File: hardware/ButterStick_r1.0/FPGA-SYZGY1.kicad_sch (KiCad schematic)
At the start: 4 parts, among them U4 ECP5UM5G_85_CABGA381

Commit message: hw.r1d0: Update BOM fieids in schematic.
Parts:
- C158, C28: Mfg Samsung Electro-Mechanics -> Yageo; PN CL05B103KP5NNNC -> CC0402KRX5R6BB104; SN-DK 1276-1002-1-ND -> (none); Tol (none) -> 10V / X5R
- C27: Mfg Samsung Electro-Mechanics -> Yageo; PN CL05B104KP5NNNC -> CC0402KRX5R5BB474; SN-DK 1276-1002-1-ND -> (none)
- U4: Mfg (none) -> Lattice Semiconductor Corporation; PN (none) -> LFE5UM5G-85F-8BG381C; manf# ECP5UM5G_85 -> (none)
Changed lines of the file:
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@@
 (kicad_sch (version 20200618) (host eeschema "5.99.0-unknown-73168a9~101~ubuntu18.04.1")
-  (page 10 18)
+  (page 1 18)
   (paper "A4")
   (title_block
@@
       (effects (font (size 1.27 1.27)) hide)
     )
-    (property "SN-DK" "1276-1002-1-ND" (id 4) (at 16.51 246.38 0)
-      (effects (font (size 1.27 1.27)) hide)
-    )
-    (property "PN" "CL05B104KP5NNNC" (id 5) (at 16.51 246.38 0)
-      (effects (font (size 1.27 1.27)) hide)
-    )
-    (property "Mfg" "Samsung Electro-Mechanics" (id 6) (at 19.05 245.11 0)
+    (property "SN-DK" "" (id 4) (at 16.51 246.38 0)
+      (effects (font (size 1.27 1.27)) hide)
+    )
+    (property "PN" "CC0402KRX5R5BB474" (id 5) (at 16.51 246.38 0)
+      (effects (font (size 1.27 1.27)) hide)
+    )
+    (property "Mfg" "Yageo" (id 6) (at 19.05 245.11 0)
       (effects (font (size 1.27 1.27)) hide)
     )
@@
       (effects (font (size 1.27 1.27)) hide)
     )
-    (property "SN-DK" "1276-1002-1-ND" (id 4) (at 26.67 246.38 0)
-      (effects (font (size 1.27 1.27)) hide)
-    )
-    (property "PN" "CL05B103KP5NNNC" (id 5) (at 26.67 246.38 0)
-      (effects (font (size 1.27 1.27)) hide)
-    )
-    (property "Mfg" "Samsung Electro-Mechanics" (id 6) (at 19.05 245.11 0)
+    (property "SN-DK" "" (id 4) (at 26.67 246.38 0)
+      (effects (font (size 1.27 1.27)) hide)
+    )
+    (property "PN" "CC0402KRX5R6BB104" (id 5) (at 26.67 246.38 0)
+      (effects (font (size 1.27 1.27)) hide)
+    )
+    (property "Mfg" "Yageo" (id 6) (at 19.05 245.11 0)
+      (effects (font (size 1.27 1.27)) hide)
+    )
+    (property "Tol" "10V / X5R" (id 4) (at 176.53 69.85 0)
       (effects (font (size 1.27 1.27)) hide)
     )
@@
       (effects (font (size 1.27 1.27)) hide)
     )
-    (property "SN-DK" "1276-1002-1-ND" (id 4) (at 36.83 246.38 0)
-      (effects (font (size 1.27 1.27)) hide)
-    )
-    (property "PN" "CL05B103KP5NNNC" (id 5) (at 36.83 246.38 0)
-      (effects (font (size 1.27 1.27)) hide)
-    )
-    (property "Mfg" "Samsung Electro-Mechanics" (id 6) (at 29.21 245.11 0)
+    (property "SN-DK" "" (id 4) (at 36.83 246.38 0)
+      (effects (font (size 1.27 1.27)) hide)
+    )
+    (property "PN" "CC0402KRX5R6BB104" (id 5) (at 36.83 246.38 0)
+      (effects (font (size 1.27 1.27)) hide)
+    )
+    (property "Mfg" "Yageo" (id 6) (at 29.21 245.11 0)
+      (effects (font (size 1.27 1.27)) hide)
+    )
+    (property "Tol" "10V / X5R" (id 4) (at 186.69 69.85 0)
       (effects (font (size 1.27 1.27)) hide)
     )
@@
       (effects (font (size 1.524 1.524)) (justify right) hide)
     )
-    (property "manf#" "ECP5UM5G_85" (id 4) (at 123.19 72.39 0)
+    (property "manf#" "" (id 4) (at 123.19 72.39 0)
       (effects (font (size 1.524 1.524)) (justify right) hide)
     )
-  )
+    (property "Mfg" "Lattice Semiconductor Corporation" (id 4) (at 119.38 71.12 0)
+      (effects (font (size 1.27 1.27)) hide)
+    )
+    (property "PN" "LFE5UM5G-85F-8BG381C" (id 5) (at 119.38 71.12 0)
+      (effects (font (size 1.27 1.27)) hide)
+    )
+  )

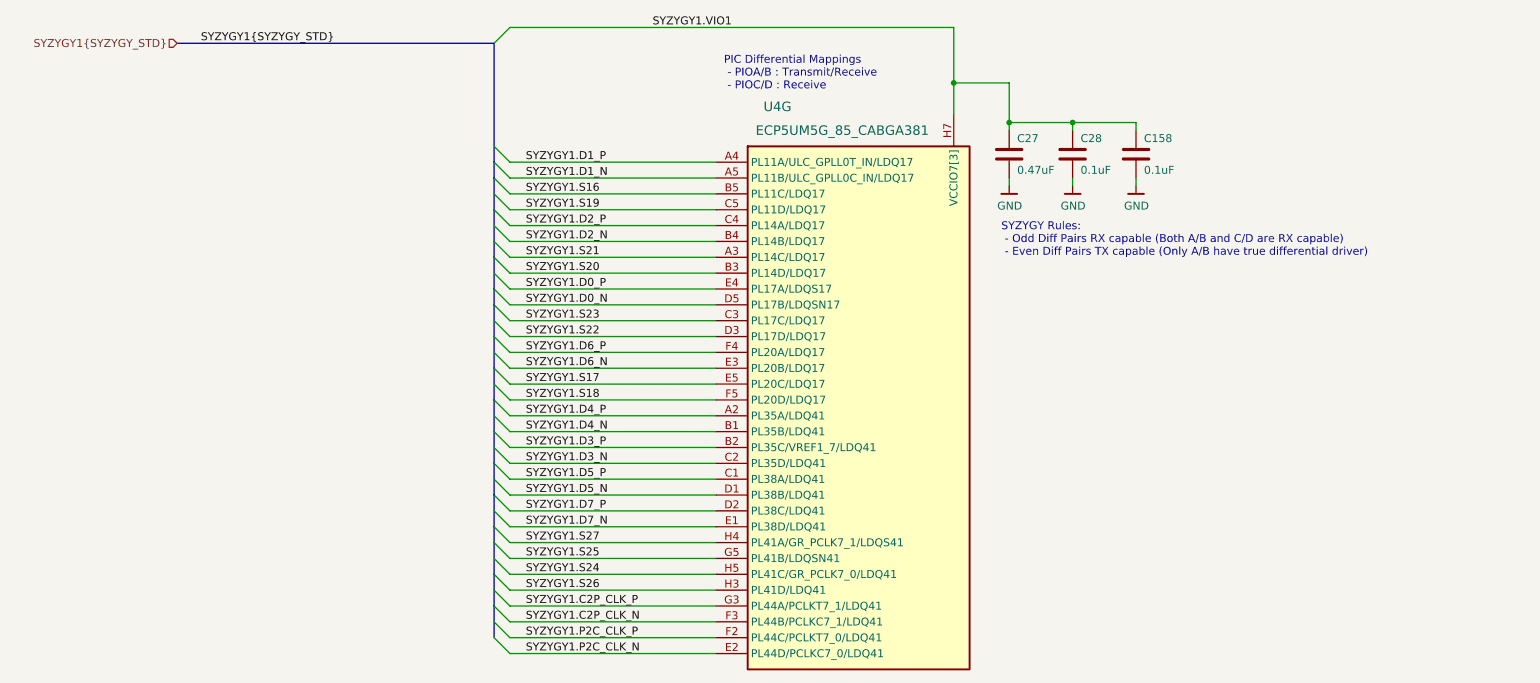
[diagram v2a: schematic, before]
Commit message: hw.r1d0: Fix RGMII straps
This commit correctly sets the stop resistos on the RGMII lines to 1K5
instead of DNP.
Also regenerate and add a schematic in PDF format.

Fixes #6
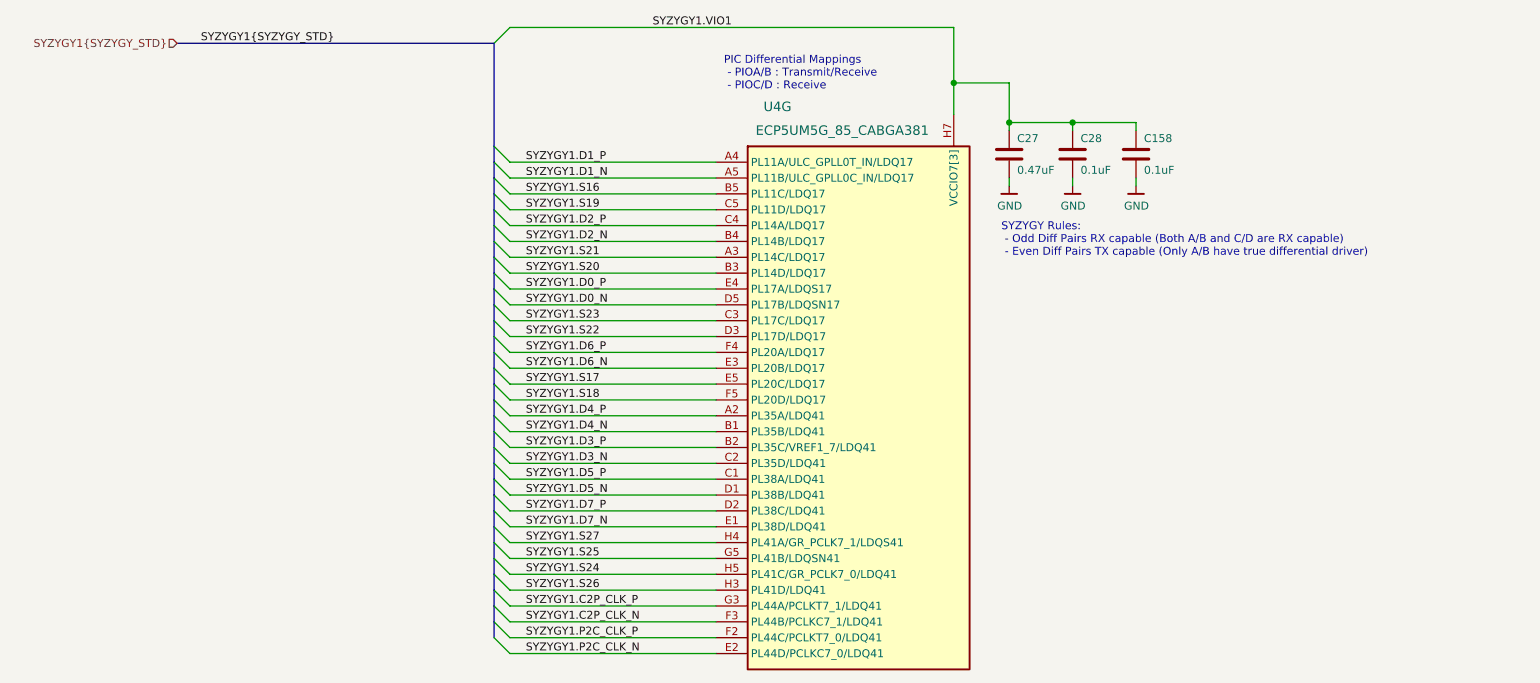
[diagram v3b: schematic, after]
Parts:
- U4: PN LFE5UM5G-85F-8BG381C -> LFE5UM5G-85F-8BG381I
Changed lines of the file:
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@@
-(kicad_sch (version 20200618) (host eeschema "5.99.0-unknown-73168a9~101~ubuntu18.04.1")
+(kicad_sch (version 20201015) (generator eeschema)
   (page 1 18)
   (paper "A4")
   (title_block
     (title "ButterStick")
-    (date "2020-07-17")
+    (date "2020-11-01")
     (rev "r1.0")
     (company "GsD")
     (comment 1 "Functional prototyping board for the Lattice ECP5.")
-  )
-  (junction (at 157.48 58.42) (diameter 0) (color 0 0 0 0))
-  (junction (at 166.37 64.77) (diameter 0) (color 0 0 0 0))
-  (junction (at 176.53 64.77) (diameter 0) (color 0 0 0 0))
+    (comment 2 "SYZYGY compatible")
+  )
+  (junction (at 157.48 58.42) (diameter 1.016) (color 0 0 0 0))
+  (junction (at 166.37 64.77) (diameter 1.016) (color 0 0 0 0))
+  (junction (at 176.53 64.77) (diameter 1.016) (color 0 0 0 0))
   (bus_entry (at 83.82 52.07) (size 2.54 -2.54)
     (stroke (width 0.1524) (type solid) (color 0 0 0 0))
@@
     (stroke (width 0) (type solid) (color 0 0 0 0))
   )
-  (bus (pts (xy 83.82 52.07) (xy 83.82 71.12))
+  (bus (pts (xy 83.82 52.07) (xy 83.82 68.58))
+    (stroke (width 0) (type solid) (color 0 0 0 0))
+  )
+  (bus (pts (xy 83.82 68.58) (xy 83.82 71.12))
     (stroke (width 0) (type solid) (color 0 0 0 0))
   )
@@
     (stroke (width 0) (type solid) (color 0 0 0 0))
   )
-  (bus (pts (xy 83.82 73.66) (xy 83.82 78.74))
-    (stroke (width 0) (type solid) (color 0 0 0 0))
-  )
-  (bus (pts (xy 83.82 78.74) (xy 83.82 83.82))
+  (bus (pts (xy 83.82 73.66) (xy 83.82 76.2))
+    (stroke (width 0) (type solid) (color 0 0 0 0))
+  )
+  (bus (pts (xy 83.82 76.2) (xy 83.82 78.74))
+    (stroke (width 0) (type solid) (color 0 0 0 0))
+  )
+  (bus (pts (xy 83.82 78.74) (xy 83.82 81.28))
+    (stroke (width 0) (type solid) (color 0 0 0 0))
+  )
+  (bus (pts (xy 83.82 81.28) (xy 83.82 83.82))
     (stroke (width 0) (type solid) (color 0 0 0 0))
   )
@@
     (stroke (width 0) (type solid) (color 0 0 0 0))
   )
-  (bus (pts (xy 83.82 86.36) (xy 83.82 91.44))
+  (bus (pts (xy 83.82 86.36) (xy 83.82 88.9))
+    (stroke (width 0) (type solid) (color 0 0 0 0))
+  )
+  (bus (pts (xy 83.82 88.9) (xy 83.82 91.44))
     (stroke (width 0) (type solid) (color 0 0 0 0))
   )
@@
     (stroke (width 0) (type solid) (color 0 0 0 0))
   )
-  (bus (pts (xy 83.82 93.98) (xy 83.82 99.06))
-    (stroke (width 0) (type solid) (color 0 0 0 0))
-  )
-  (bus (pts (xy 83.82 99.06) (xy 83.82 104.14))
-    (stroke (width 0) (type solid) (color 0 0 0 0))
-  )
-  (bus (pts (xy 83.82 104.14) (xy 83.82 109.22))
-    (stroke (width 0) (type solid) (color 0 0 0 0))
-  )
-  (bus (pts (xy 83.82 109.22) (xy 83.82 114.3))
-    (stroke (width 0) (type solid) (color 0 0 0 0))
-  )
-  (bus (pts (xy 83.82 114.3) (xy 83.82 119.38))
-    (stroke (width 0) (type solid) (color 0 0 0 0))
-  )
-  (bus (pts (xy 83.82 119.38) (xy 83.82 124.46))
-    (stroke (width 0) (type solid) (color 0 0 0 0))
-  )
-  (bus (pts (xy 83.82 124.46) (xy 83.82 129.54))
+  (bus (pts (xy 83.82 93.98) (xy 83.82 96.52))
+    (stroke (width 0) (type solid) (color 0 0 0 0))
+  )
+  (bus (pts (xy 83.82 96.52) (xy 83.82 99.06))
+    (stroke (width 0) (type solid) (color 0 0 0 0))
+  )
+  (bus (pts (xy 83.82 99.06) (xy 83.82 101.6))
+    (stroke (width 0) (type solid) (color 0 0 0 0))
+  )
+  (bus (pts (xy 83.82 101.6) (xy 83.82 104.14))
+    (stroke (width 0) (type solid) (color 0 0 0 0))
+  )
+  (bus (pts (xy 83.82 104.14) (xy 83.82 106.68))
+    (stroke (width 0) (type solid) (color 0 0 0 0))
+  )
+  (bus (pts (xy 83.82 106.68) (xy 83.82 109.22))
+    (stroke (width 0) (type solid) (color 0 0 0 0))
+  )
+  (bus (pts (xy 83.82 109.22) (xy 83.82 111.76))
+    (stroke (width 0) (type solid) (color 0 0 0 0))
+  )
+  (bus (pts (xy 83.82 111.76) (xy 83.82 114.3))
+    (stroke (width 0) (type solid) (color 0 0 0 0))
+  )
+  (bus (pts (xy 83.82 114.3) (xy 83.82 116.84))
+    (stroke (width 0) (type solid) (color 0 0 0 0))
+  )
+  (bus (pts (xy 83.82 116.84) (xy 83.82 119.38))
+    (stroke (width 0) (type solid) (color 0 0 0 0))
+  )
+  (bus (pts (xy 83.82 119.38) (xy 83.82 121.92))
+    (stroke (width 0) (type solid) (color 0 0 0 0))
+  )
+  (bus (pts (xy 83.82 121.92) (xy 83.82 124.46))
+    (stroke (width 0) (type solid) (color 0 0 0 0))
+  )
+  (bus (pts (xy 83.82 124.46) (xy 83.82 127))
+    (stroke (width 0) (type solid) (color 0 0 0 0))
+  )
+  (bus (pts (xy 83.82 127) (xy 83.82 129.54))
     (stroke (width 0) (type solid) (color 0 0 0 0))
   )
@@
     (stroke (width 0) (type solid) (color 0 0 0 0))
   )
-  (bus (pts (xy 83.82 132.08) (xy 83.82 137.16))
-    (stroke (width 0) (type solid) (color 0 0 0 0))
-  )
-  (bus (pts (xy 83.82 137.16) (xy 83.82 142.24))
-    (stroke (width 0) (type solid) (color 0 0 0 0))
-  )
-  (bus (pts (xy 83.82 142.24) (xy 83.82 147.32))
+  (bus (pts (xy 83.82 132.08) (xy 83.82 134.62))
+    (stroke (width 0) (type solid) (color 0 0 0 0))
+  )
+  (bus (pts (xy 83.82 134.62) (xy 83.82 137.16))
+    (stroke (width 0) (type solid) (color 0 0 0 0))
+  )
+  (bus (pts (xy 83.82 137.16) (xy 83.82 139.7))
+    (stroke (width 0) (type solid) (color 0 0 0 0))
+  )
+  (bus (pts (xy 83.82 139.7) (xy 83.82 142.24))
+    (stroke (width 0) (type solid) (color 0 0 0 0))
+  )
+  (bus (pts (xy 83.82 142.24) (xy 83.82 144.78))
+    (stroke (width 0) (type solid) (color 0 0 0 0))
+  )
+  (bus (pts (xy 83.82 144.78) (xy 83.82 147.32))
     (stroke (width 0) (type solid) (color 0 0 0 0))
   )
@@
       (effects (font (size 1.524 1.524)) (justify right) hide)
     )
+    (property "PN" "LFE5UM5G-85F-8BG381I" (id 5) (at 119.38 71.12 0)
+      (effects (font (size 1.27 1.27)) hide)
+    )
     (property "Mfg" "Lattice Semiconductor Corporation" (id 4) (at 119.38 71.12 0)
       (effects (font (size 1.27 1.27)) hide)
     )
-    (property "PN" "LFE5UM5G-85F-8BG381C" (id 5) (at 119.38 71.12 0)
-      (effects (font (size 1.27 1.27)) hide)
-    )
